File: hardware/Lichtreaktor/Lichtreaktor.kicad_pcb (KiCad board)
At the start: 2 copper layers, 90 x 90 mm, 72 parts, among them Q1 BC337, Q2 BC337, Q3 BC337, Q4 BC337, Q5 BC337, Q6 BC337, SW1 EC11E18244A5, U1 XIAO-RP2040-DIP

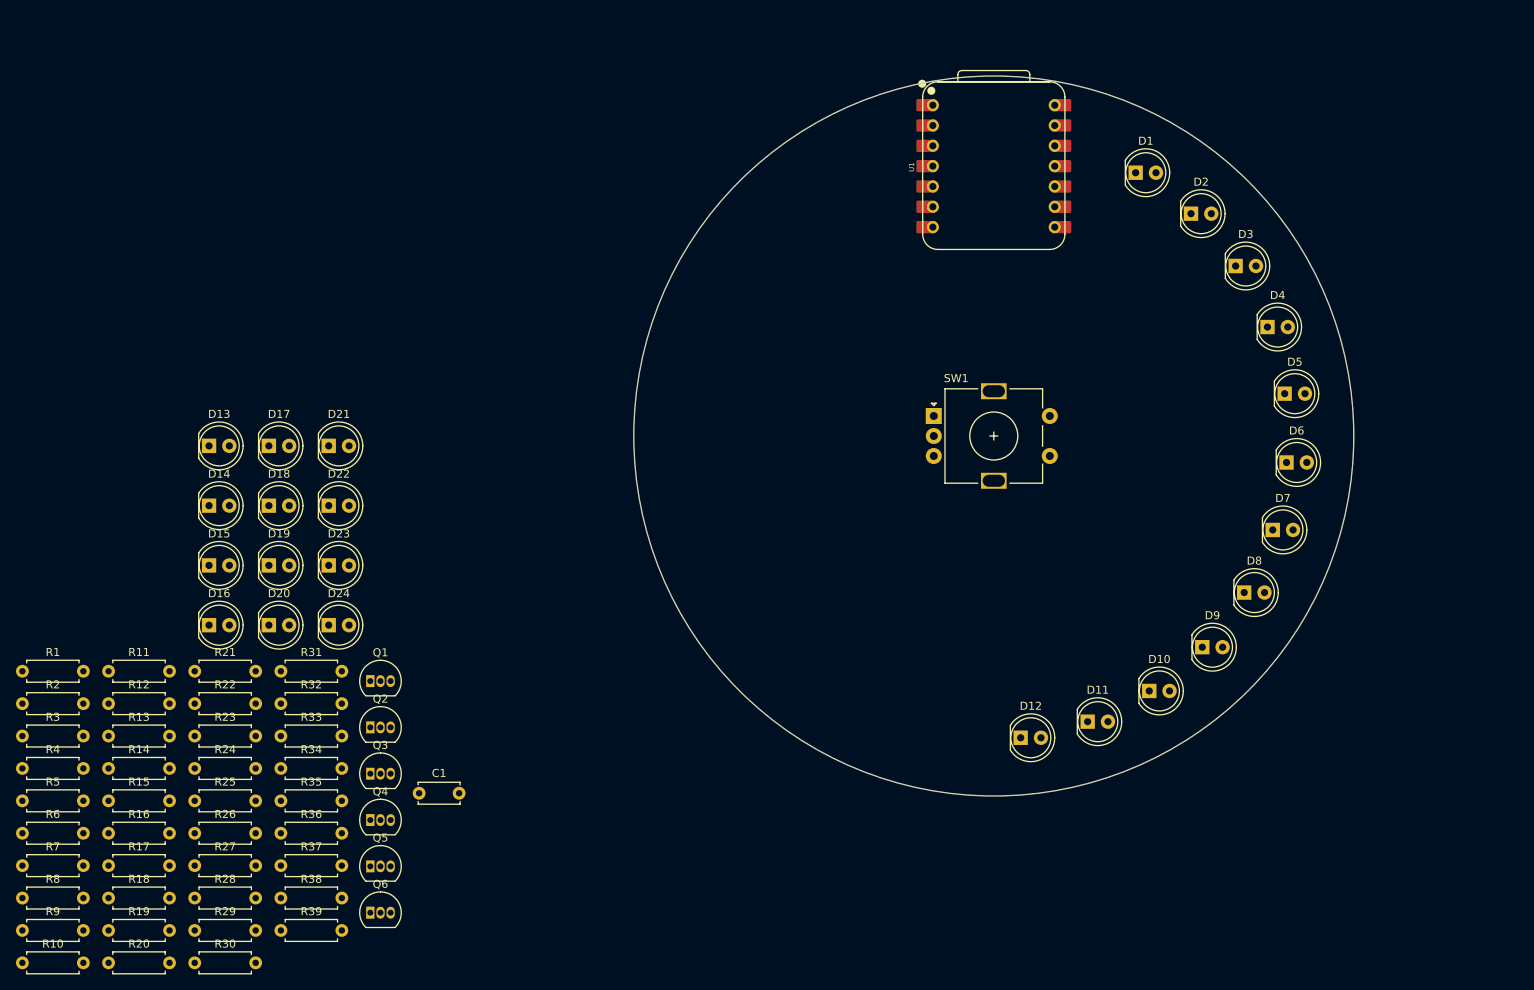
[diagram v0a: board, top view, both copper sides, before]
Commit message: Complete PCB routing and ground pours, update project README
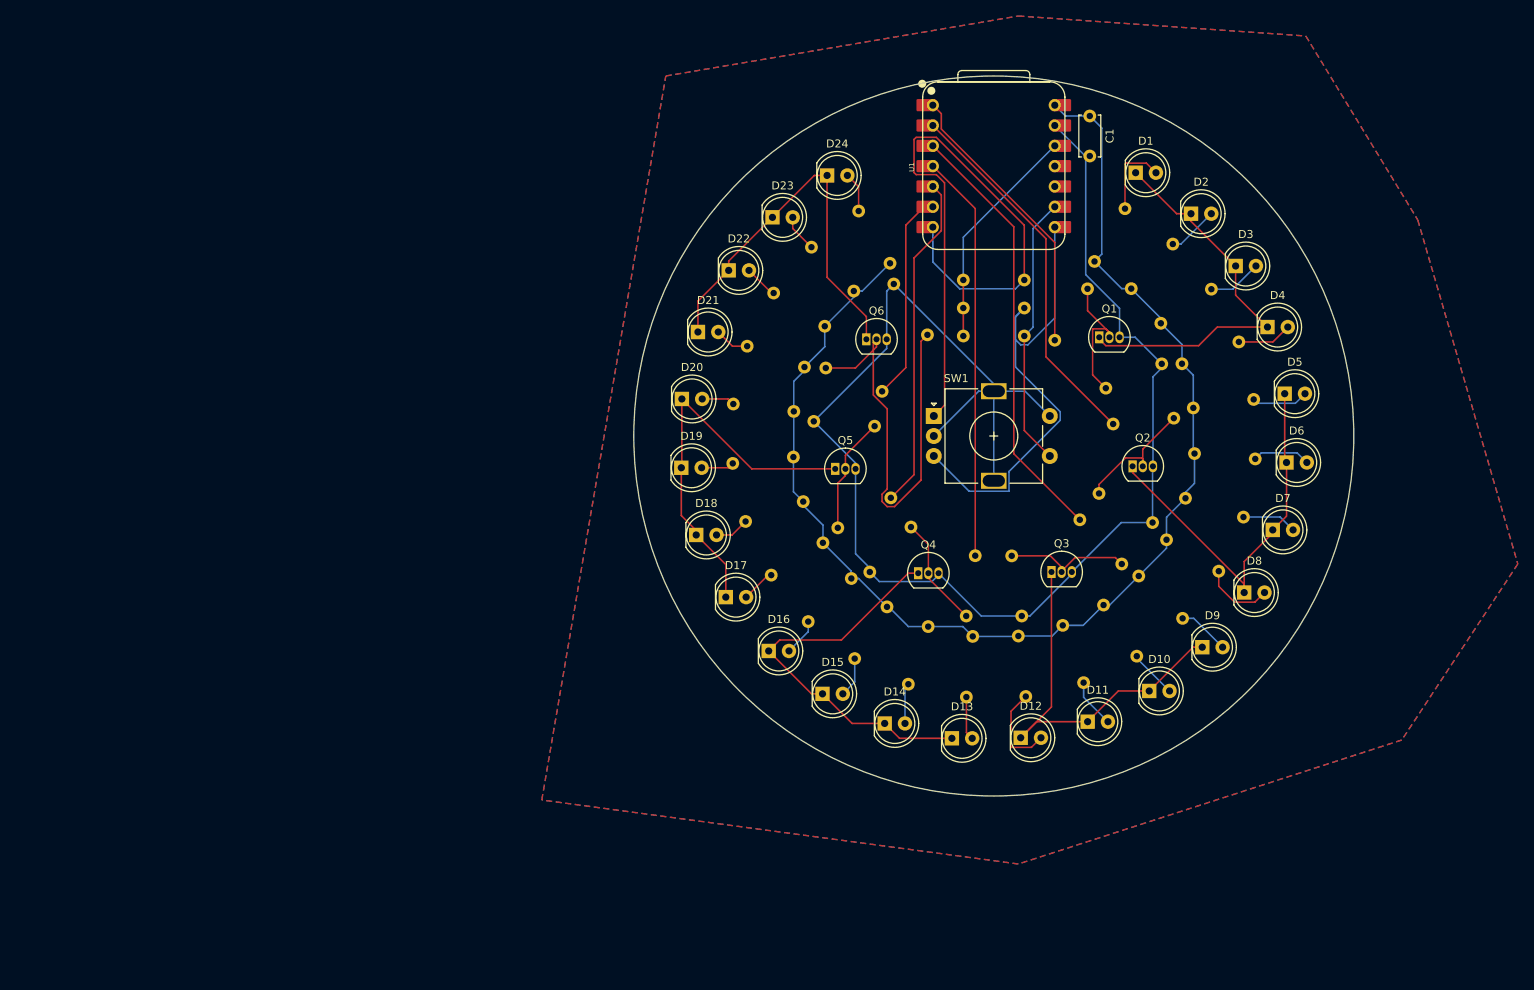
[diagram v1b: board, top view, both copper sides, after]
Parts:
- R1, R10, R11, R12, R13, R14, R15, R16, R17, R18, R19, R2, R20, R21, R22, R23, R24, R25, R26, R27, R28, R29, R3, R30, R31, R32, R33, R34, R35, R36, R37, R38, R39, R4, R5, R6, R7, R8, R9: moved to B.Cu
- moved R7 157.2 mm to (209.9, 61.5), turned to 8 degrees
- moved R8 156.7 mm to (210.1, 67.2), turned to -5 degrees
- moved R10 156.6 mm to (209.0, 72.8), turned to -18 degrees
- moved R4 153.5 mm to (208.5, 56.0), turned to 21 degrees
- moved R3 151.4 mm to (205.9, 50.9), turned to 34 degrees
- moved R9 150.3 mm to (199.9, 63.5), turned to 5.5 degrees
- moved R2 148.0 mm to (202.2, 46.6), turned to 47 degrees
- moved R6 146.4 mm to (199.0, 59.0), turned to 23.5 degrees
- moved R1 143.5 mm to (197.6, 43.2), turned to 60 degrees
- moved R5 141.3 mm to (192.6, 53.0), turned to 57.5 degrees
- moved R12 133.8 mm to (206.6, 78.0), turned to -31 degrees
- moved R13 130.3 mm to (203.1, 82.5), turned to -44 degrees
- moved R15 126.4 mm to (195.8, 75.5), turned to -46.5 degrees
- moved R14 126.0 mm to (198.7, 86.1), turned to -57 degrees
- moved R11 125.8 mm to (198.2, 72.2), turned to -28.5 degrees
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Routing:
- net /GND: track 0.00 -> 192.1 mm
- net /+5V: track 0.00 -> 162.3 mm
- net /ENC_A: track 0.00 -> 81.1 mm
- net /ENC_B: track 0.00 -> 62.1 mm
- net /BASE_G6: track 0.00 -> 54.8 mm
- net /PWM_G3: track 0.00 -> 54.4 mm
- net /PWM_G4: track 0.00 -> 50.9 mm
- net /LED_G4: track 0.00 -> 50.1 mm
- net /LED_G5: track 0.00 -> 49.9 mm
- net /LED_G1: track 0.00 -> 49.7 mm
- net /LED_G3: track 0.00 -> 49.7 mm
- net /LED_G6: track 0.00 -> 49.7 mm
- net /LED_G2: track 0.00 -> 48.7 mm
- net /PWM_G2: track 0.00 -> 46.6 mm
- net /PWM_G5: track 0.00 -> 42.0 mm
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- added copper zone on B.Cu, net /GND
- added copper zone on F.Cu, net /GND
